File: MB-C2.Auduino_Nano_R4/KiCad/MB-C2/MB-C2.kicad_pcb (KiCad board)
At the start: 2 copper layers, 47 x 72 mm, 41 parts, among them J1 PH-2x15SG, J2 PH-2x15SG, J3 Cut_of_PH-2x40RG, J4 Barrel_Jack_Switch, J5 Conn_02x04_Odd_Even, J6 Servo 3x2 header, J7 Servo 3x2 header, J8 Conn_01x04_Pin, Q1 INK021ABS1-T112, Q2 INK021ABS1-T112, Q3 INK021ABS1-T112, Q4 INK021ABS1-T112, U1 AE-G5V-DRV, U2 AE-G5V-DRV, U3 AE-G5V-DRV, U4 AE-G5V-DRV

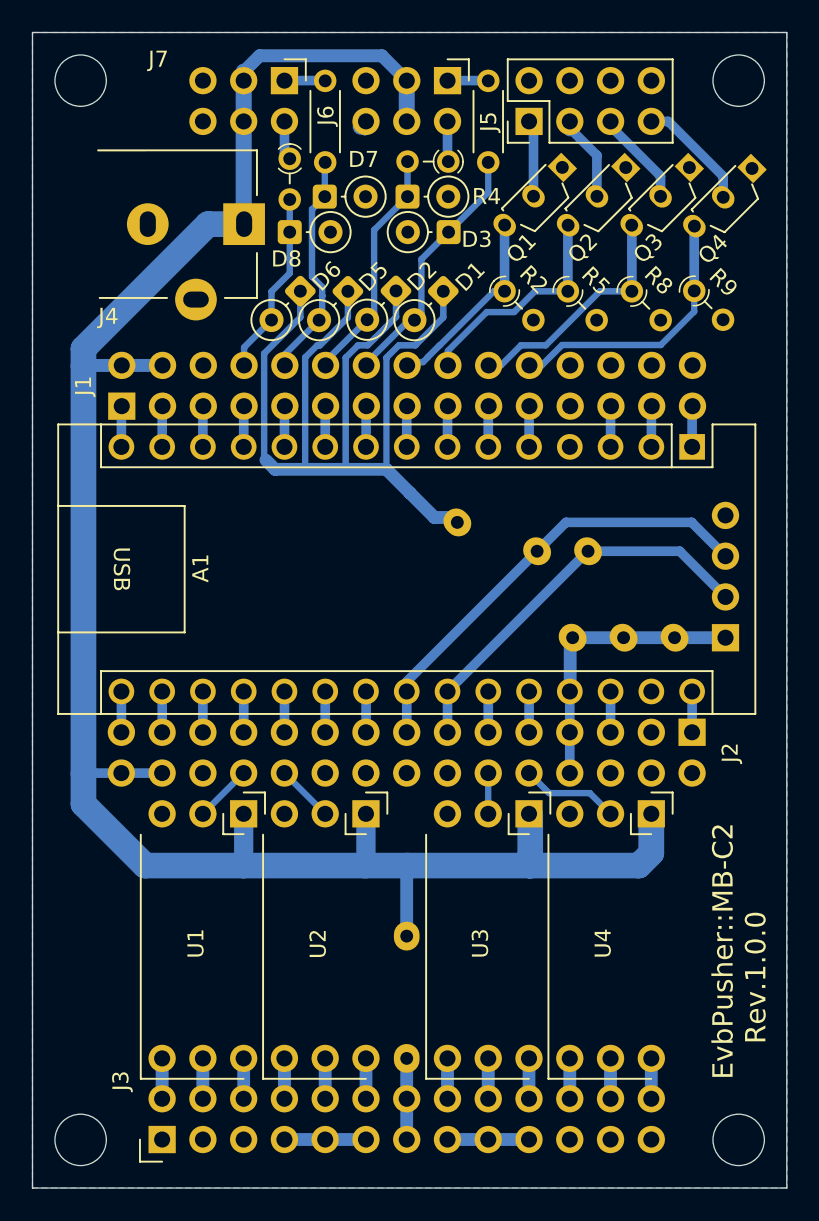
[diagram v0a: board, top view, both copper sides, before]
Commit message: [MB-C2:KiCAD] Change to double side PCB
- Change design rule to JLCPB capability.
- Remove jumper resisters.
- Migrate power lines to front side.
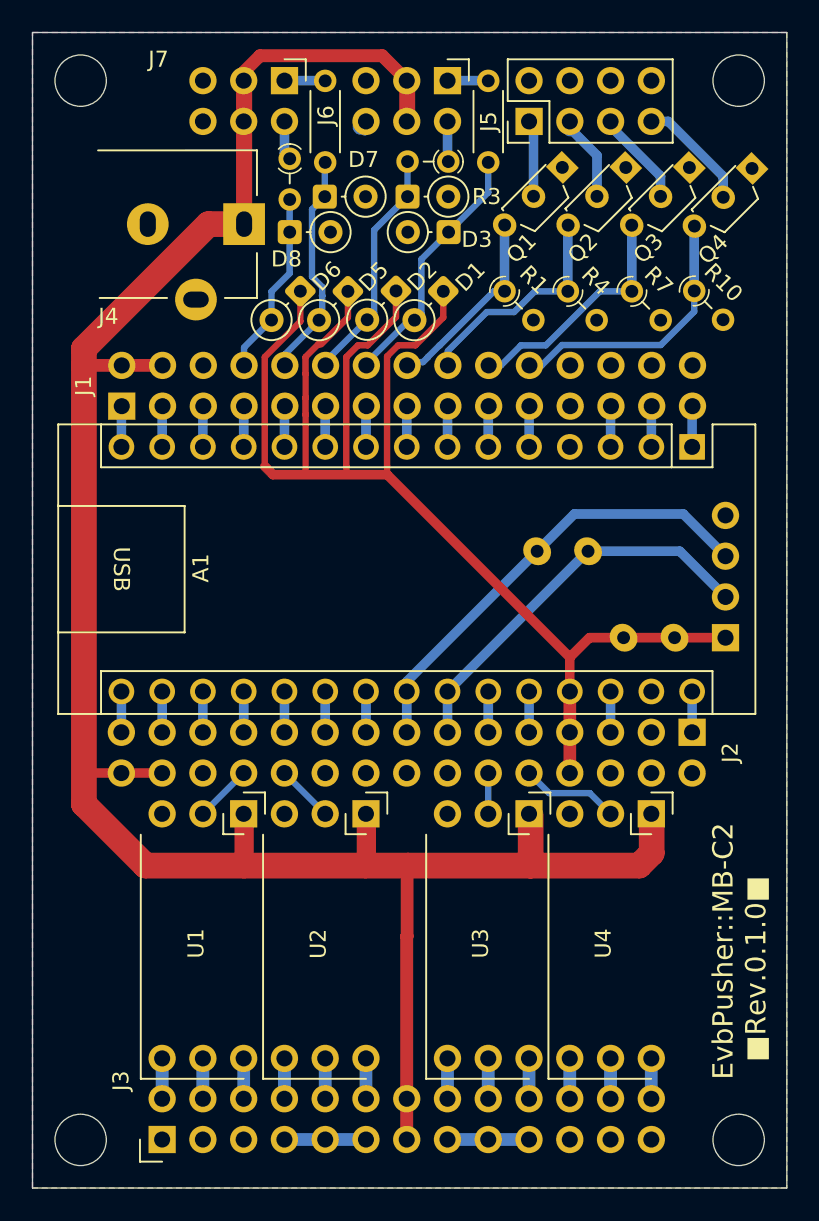
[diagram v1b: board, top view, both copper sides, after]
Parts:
- removed the R1 at (133.7, 115.7)
- removed the R10 at (123.3, 141.9)
- R8: renamed from R11; value 0 -> 4.7k
- R9: renamed from R12; value 0 -> 4.7k
- renumbered R2 to R1, R9 to R10, R3 to R2, R4 to R3, R5 to R4, R6 to R5, R7 to R6, R8 to R7
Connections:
- D1 pad 1: Net-(D1-K) -> /PIN27_5V
- D2 pad 1: Net-(D1-K) -> /PIN27_5V
- D5 pad 1: Net-(D1-K) -> /PIN27_5V
- D6 pad 1: Net-(D1-K) -> /PIN27_5V
- J3 pad 13: Net-(J3-Pin_13) -> +5VP
- J3 pad 14: Net-(J3-Pin_13) -> +5VP
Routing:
- net /PIN27_5V: track 18.0 -> 92.4 mm
- net Net-(D1-K): track 62.8 -> 0.00 mm
- net +5VP: track 128.6 -> 140.6 mm
- net Net-(J3-Pin_13): track 5.05 -> 0.00 mm
- added copper zone on F.Cu, net GND
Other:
- board text added: "EvbPusher::MB-C2 ■Rev.0.1.0■"
- board text removed: "EvbPusher::MB-C2 Rev.1.0.0"
